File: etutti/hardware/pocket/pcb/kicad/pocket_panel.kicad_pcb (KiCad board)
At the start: 2 copper layers, 30 x 13 mm, 14 parts, among them J1 TYPE-C-31-M-12, J2 SJ1-3525N

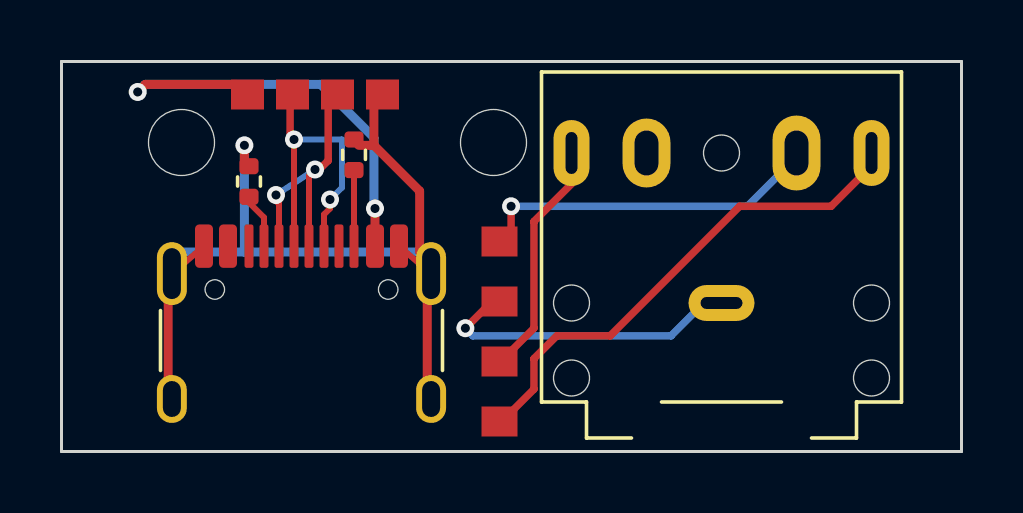
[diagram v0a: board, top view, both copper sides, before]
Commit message: eTuttino Pocket SPEC v4: F1 case finish + F2 boards closed, kit BOM
Co-Authored-By: Claude Opus 5.5 <noreply@anthropic.com>
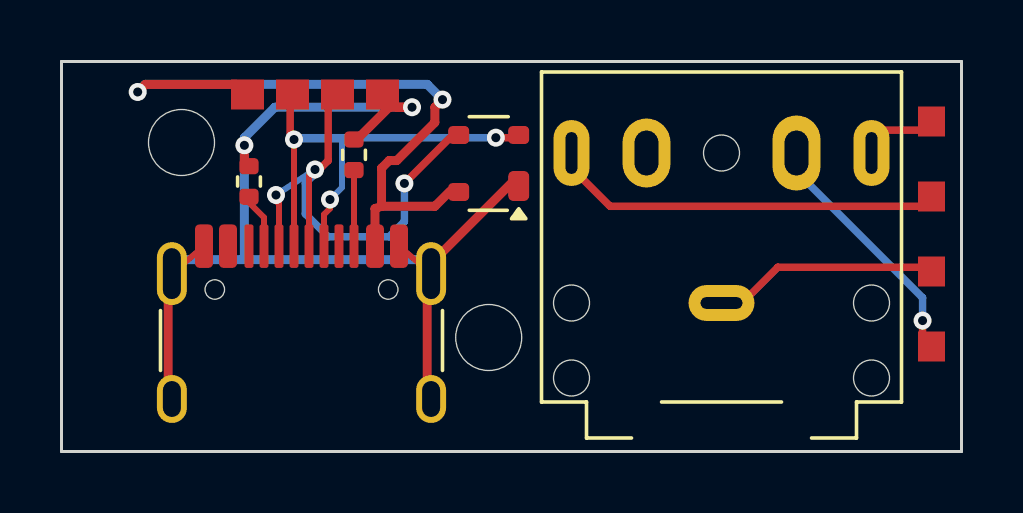
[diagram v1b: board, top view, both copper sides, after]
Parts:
- added U1: PRTR5V0U2X, SOT-143, F.Cu at (14.2, 3.40)
- moved TP5 17.5 mm to (29.0, 2.00)
- moved TP6 15.4 mm to (29.0, 4.50)
- moved TP8 14.8 mm to (29.0, 9.50)
- moved TP7 14.4 mm to (29.0, 7.00)
- moved H2 6.50 mm to (14.2, 9.20)
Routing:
- net HP_L: track 15.5 -> 1.27 mm
- net DM: track 8.07 -> 17.1 mm, vias 2 -> 3
- net DP: track 9.97 -> 17.3 mm, vias 2 -> 3
- net VBUS: track 15.7 -> 22.4 mm
- net GND: track 26.3 -> 32.5 mm, vias 1 -> 2
- net HP_R: track 6.43 -> 11.9 mm
- net HP_TIPSW: track 10.1 -> 6.66 mm
- net HP_VGND: track 9.12 -> 6.26 mm, vias 1 -> 0
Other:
- board text added: "PANEL v0.2"
- board text removed: "PANEL v0.1"
